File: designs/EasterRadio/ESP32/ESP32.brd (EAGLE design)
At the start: 30.5 x 45.5 mm, 19 parts, among them IC1 ESP32-WROVER-E

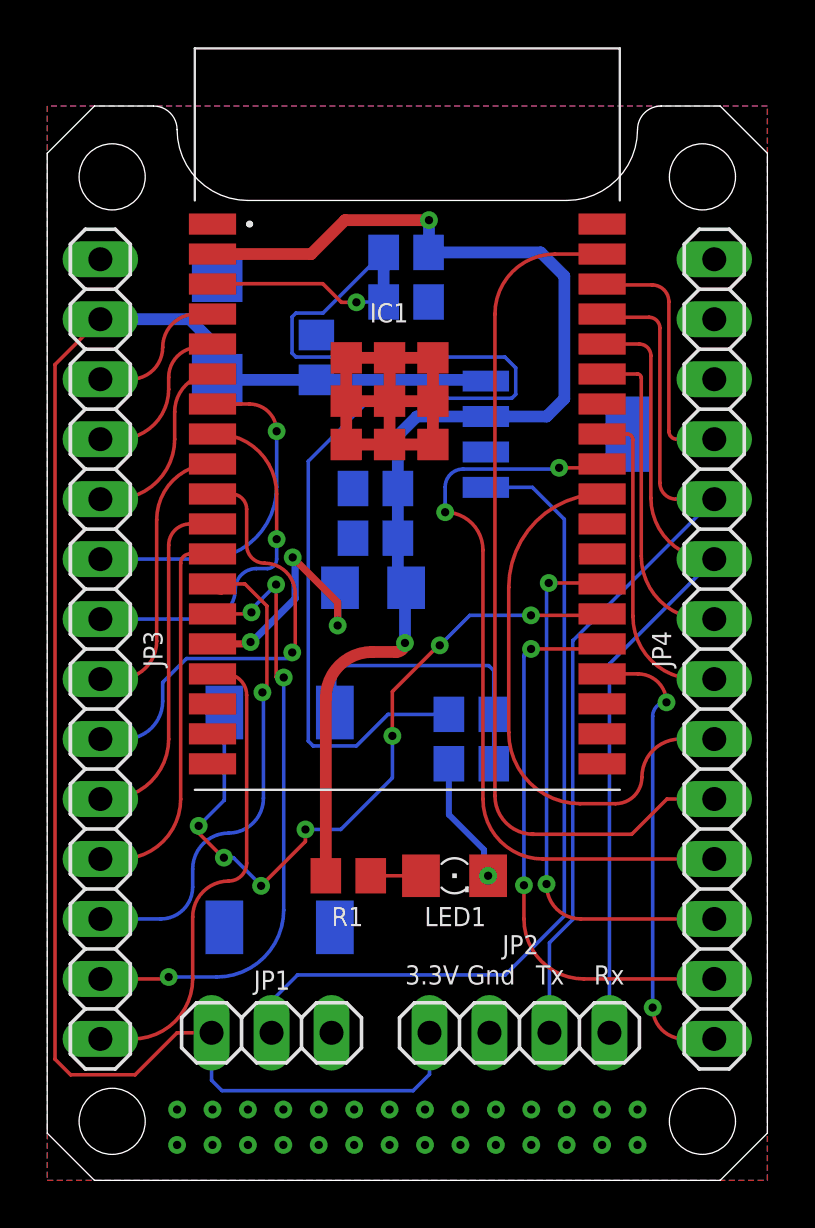
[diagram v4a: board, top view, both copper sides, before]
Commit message: added esd for rs232 to can
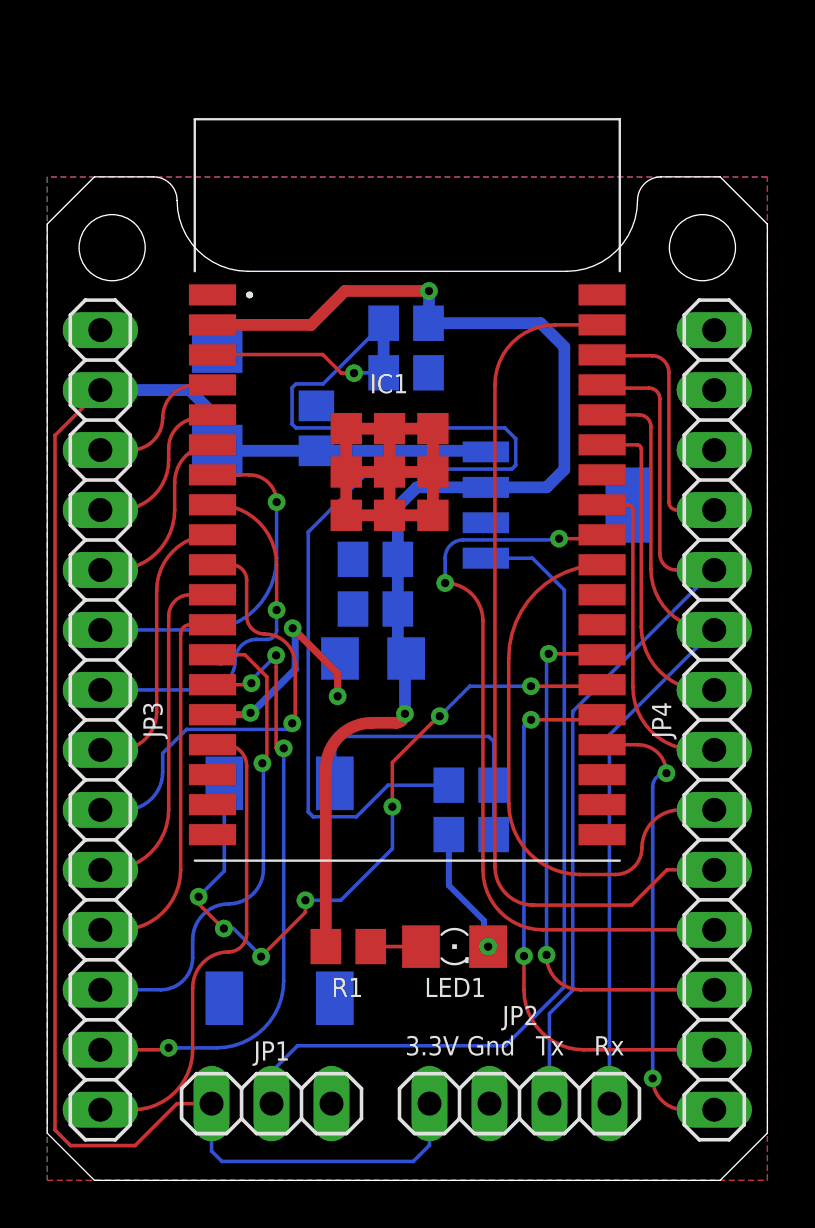
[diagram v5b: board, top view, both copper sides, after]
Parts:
- moved C1 3.00 mm to (13.8, 22.1)
- moved C2 3.00 mm to (13.9, 26.3)
- moved C3 3.00 mm to (13.9, 24.2)
- moved C4 3.00 mm to (15.2, 34.2)
- moved C5 3.00 mm to (11.4, 31.9)
- moved C6 3.00 mm to (18.0, 14.6)
- moved D1 3.00 mm to (7.20, 33.1)
- moved IC1 3.00 mm to (14.5, 30.0)
- moved JP1 3.00 mm to (9.50, 3.25)
- moved JP2 3.00 mm to (20.0, 3.25)
- moved JP3 3.00 mm to (2.25, 19.5)
- moved JP4 3.00 mm to (28.2, 19.5)
- moved LED1 3.00 mm to (17.2, 9.90)
- moved PS1 3.00 mm to (21.6, 28.6)
- moved R1 3.00 mm to (12.8, 9.90)
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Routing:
- net GND: vias 32 -> 4
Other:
- board size 30.5 x 45.5 mm -> 30.5 x 42.5 mm

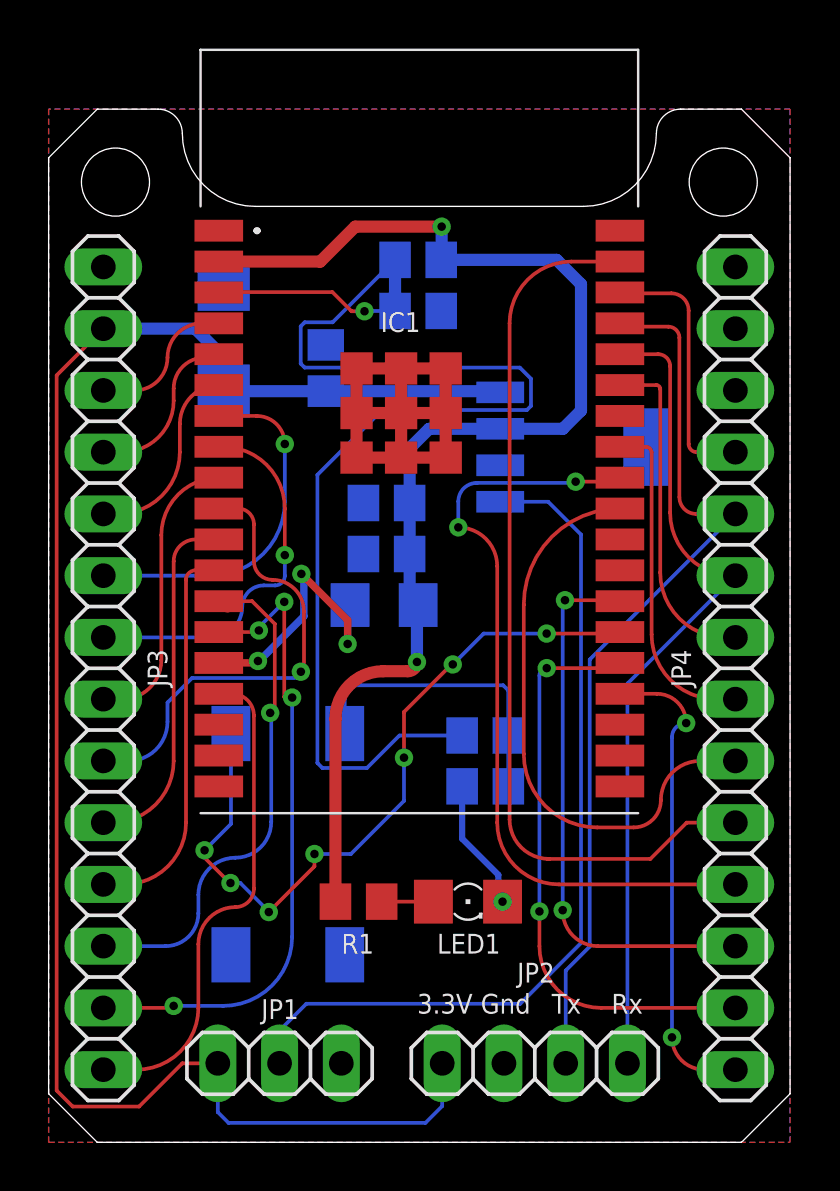
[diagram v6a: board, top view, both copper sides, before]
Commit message: added new design of radio parts added 3.3V mark
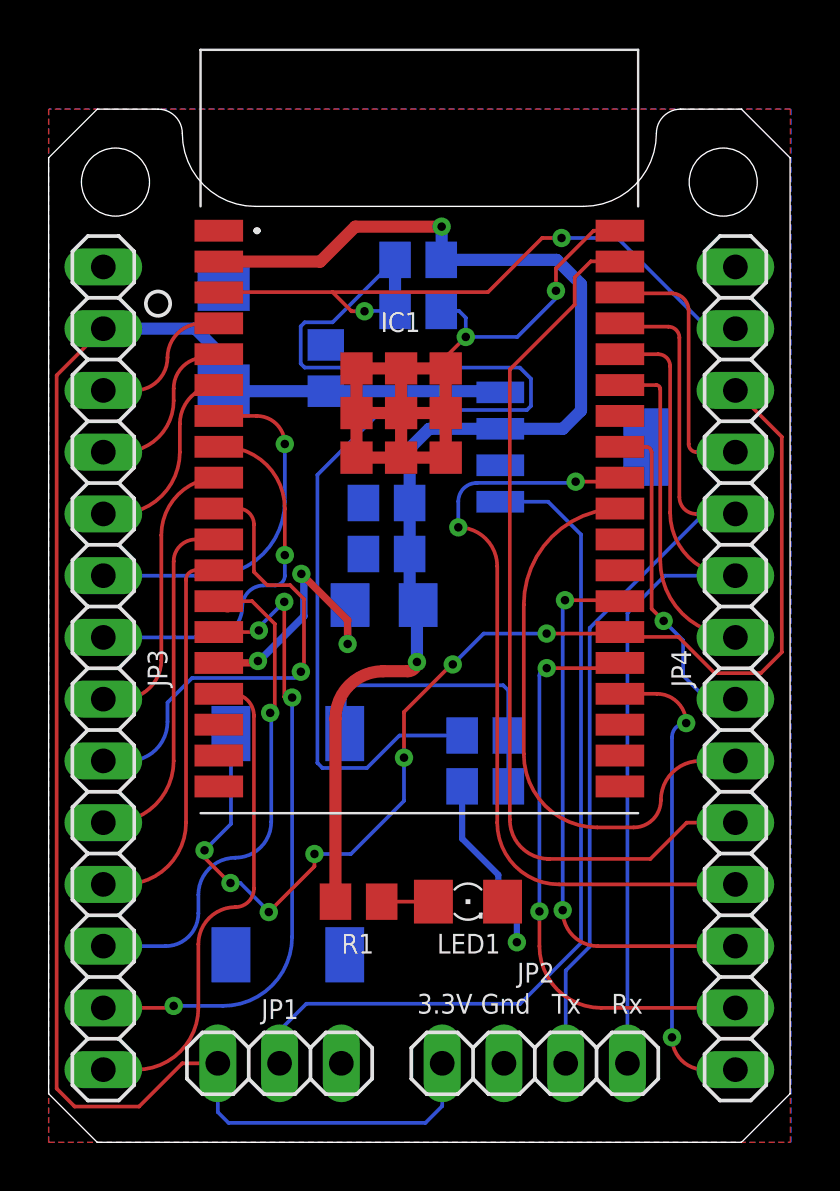
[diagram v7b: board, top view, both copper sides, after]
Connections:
- removed net IO1: IC1.25, S1.2
- new net IO0: IC1.25, JP4.12, S1.2
- net EN: now also JP4.13
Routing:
- net IO0: track 0.00 -> 50.1 mm, vias 0 -> 7
- net IO1: track 30.8 -> 0.00 mm, vias 7 -> 0
- net EN: track 55.5 -> 74.5 mm, vias 1 -> 2
- net GND: track 38.9 -> 53.2 mm, vias 4 -> 6
- net RXD0: track 34.0 -> 35.7 mm
- net ENC_2: track 13.4 -> 14.4 mm, vias 0 -> 1
- net TXD0: track 37.3 -> 38.1 mm
- net IO25: track 19.0 -> 19.6 mm

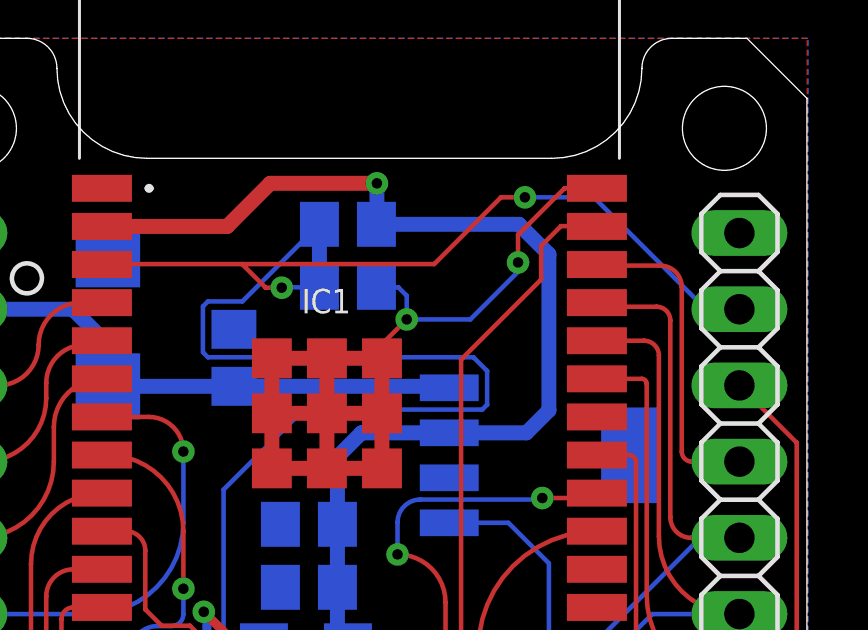
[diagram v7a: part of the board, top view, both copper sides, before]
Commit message: added final revisions to amplifier power radio ic and control pcbs
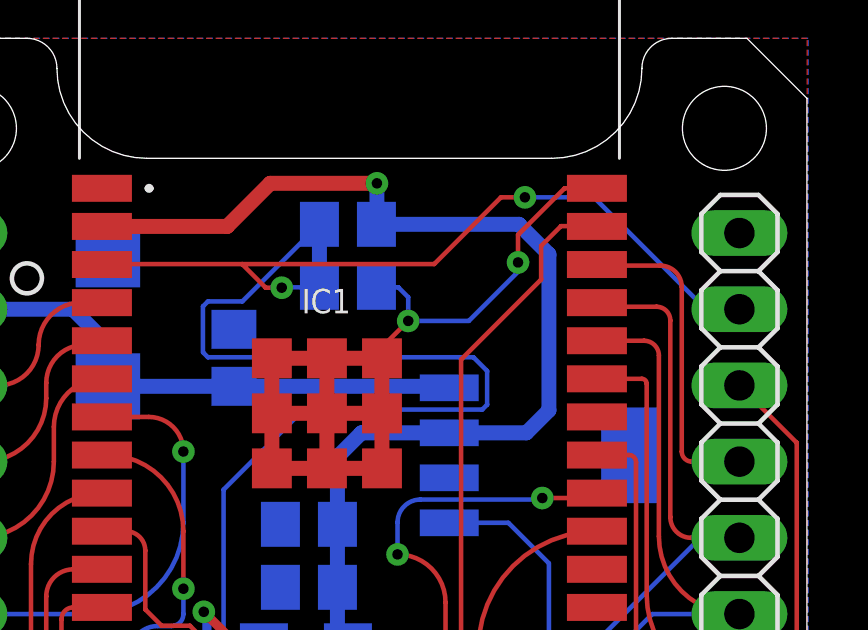
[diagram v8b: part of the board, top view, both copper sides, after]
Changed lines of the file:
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@@
 <wire x1="8.53220625" y1="19.7222" x2="7.0022" y2="19.7222" width="0.3048" layer="1"/>
 <wire x1="10.5" y1="21.64079375" x2="10.5" y2="23.27930625" width="0.3048" layer="16"/>
-<wire x1="16.335" y1="31.835" x2="16.335" y2="32.305" width="0.1524" layer="1"/>
-<wire x1="16.335" y1="32.305" x2="17.16" y2="33.13" width="0.1524" layer="1"/>
-<via x="17.16" y="33.13" extent="1-16" drill="0.35"/>
-<wire x1="17.16" y1="33.13" x2="17.16" y2="33.92" width="0.1524" layer="16"/>
+<wire x1="16.335" y1="31.835" x2="16.335" y2="32.205" width="0.1524" layer="1"/>
+<wire x1="16.335" y1="32.205" x2="17.21" y2="33.08" width="0.1524" layer="1"/>
+<via x="17.21" y="33.08" extent="1-16" drill="0.35"/>
+<wire x1="17.21" y1="33.08" x2="17.21" y2="33.87" width="0.1524" layer="16"/>
 <wire x1="16.88" y1="34.2" x2="16.15" y2="34.2" width="0.1524" layer="16"/>
-<wire x1="17.16" y1="33.92" x2="16.88" y2="34.2" width="0.1524" layer="16"/>
-<wire x1="17.16" y1="33.13" x2="19.28" y2="33.13" width="0.1524" layer="16"/>
+<wire x1="17.21" y1="33.87" x2="16.88" y2="34.2" width="0.1524" layer="16"/>
+<wire x1="17.21" y1="33.08" x2="19.23" y2="33.08" width="0.1524" layer="16"/>
 <wire x1="20.87" y1="34.72" x2="20.87" y2="35.03" width="0.1524" layer="16"/>
 <via x="20.87" y="35.03" extent="1-16" drill="0.35"/>
-<wire x1="19.28" y1="33.13" x2="20.87" y2="34.72" width="0.1524" layer="16"/>
+<wire x1="19.23" y1="33.08" x2="20.87" y2="34.72" width="0.1524" layer="16"/>
 <wire x1="20.87" y1="35.03" x2="20.87" y2="35.95" width="0.1524" layer="1"/>
 <wire x1="22.42" y1="37.5" x2="23.5" y2="37.5" width="0.1524" layer="1"/>
